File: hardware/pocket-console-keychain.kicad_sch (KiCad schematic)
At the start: 14 parts, among them J1 USB-C Power In

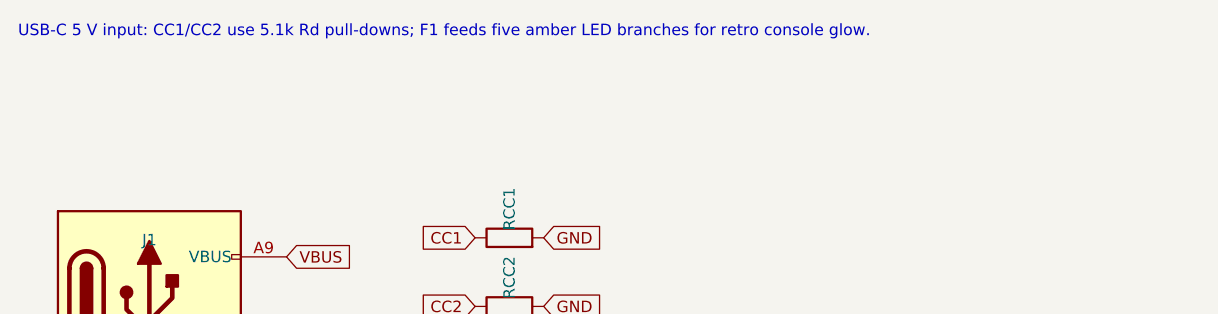
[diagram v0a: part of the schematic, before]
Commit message: Replace retro console with cleaner pocket console PCB
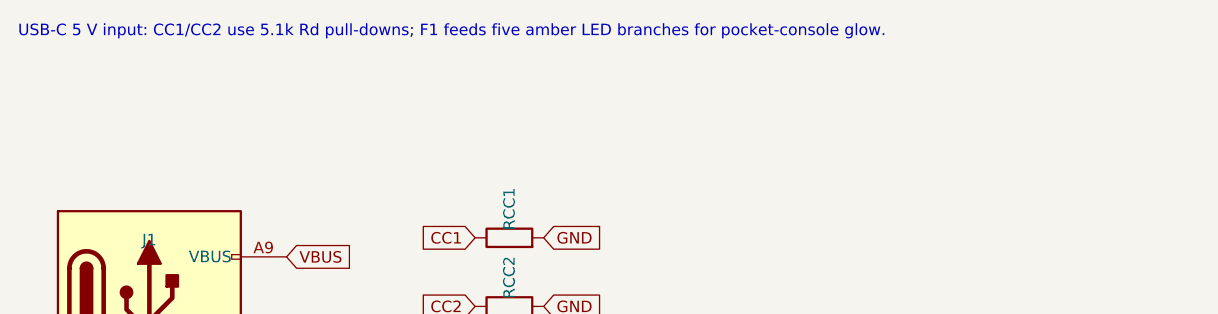
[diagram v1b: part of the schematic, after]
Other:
- note added: "USB-C 5 V input: CC1/CC2 use 5.1k Rd pull-downs; F1 feeds five amber LED branches for pocket-console glow."
- note removed: "USB-C 5 V input: CC1/CC2 use 5.1k Rd pull-downs; F1 feeds five amber LED branches for retro console glow."
- title: USB-C Retro Console PCB Keychain -> USB-C Pocket Console PCB Keychain
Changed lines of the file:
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@@
   (paper "A4")
   (title_block
-    (title "USB-C Retro Console PCB Keychain")
+    (title "USB-C Pocket Console PCB Keychain")
     (date "2026-07-27")
     (rev "B")
     (company "Open hardware concept")
-    (comment 1 "USB-C powered retro handheld PCB keychain")
+    (comment 1 "USB-C powered pocket-console LED keychain")
   )
   (global_label "CC1" (shape input) (at 55.24 63.08 0)
@@
     )
   )
-  (text "USB-C 5 V input: CC1/CC2 use 5.1k Rd pull-downs; F1 feeds five amber LED branches for retro console glow." (at 25.40 25.40 0)
-    (effects (font (size 1.27 1.27)) (justify left))
-  )
+  (text "USB-C 5 V input: CC1/CC2 use 5.1k Rd pull-downs; F1 feeds five amber LED branches for pocket-console glow." (at 25.40 25.40 0)
+    (effects (font (size 1.27 1.27)) (justify left))
+  )
